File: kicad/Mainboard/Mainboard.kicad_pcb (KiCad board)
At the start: 2 copper layers, 46.9 x 107.1 mm, 275 parts, among them J1 ESP8266 module, J10 MIC_EXT, J11 VIB2, J12 SPK_EXT, J13 GPS_CONN, J14 Micro_SD_Card, J15 DBG_CONN, J3 USB_OTG, J4 SWD, J5 BATT, J6 POT_PWR_SW, J7 Conn_01x10, J8 Antenna, J9 VIB1, Q1 BSS138, Q2 BSS138, Q3 BGA6589, Q4 BSS138, Q5 BSS138, Q6 BSS138, Q7 FDV304P, SW1 INT_PTT_SW, T1 AFT05MS004NT1, U1 STM32F777VIT, U10 LM386, U11 LSM9DS1, U13 BGA2874, U2 USBLC6-2SC6, U3 LD1117S50TR_SOT223, U4 LD1117S33TR_SOT223, U5 ADF7021, U6 HMC546MS8GETR, U7 LM2904A, U8 HEF4066B, U9 OPA340UA, X1 12.288MHz

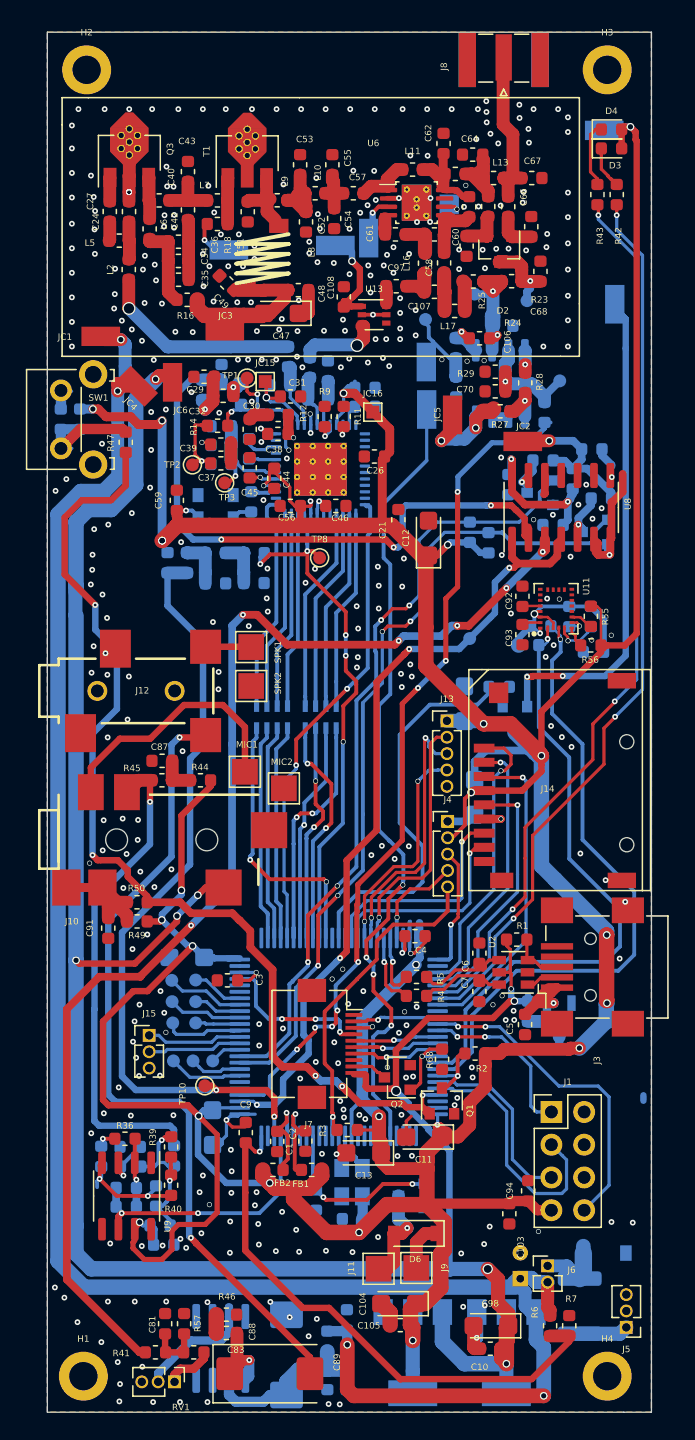
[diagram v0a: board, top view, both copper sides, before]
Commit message: added jumpers on GPIO0 and GPIO2 for ESP8266 module; described pin headers on PCB; connected pin 16 of STM32 to Power Down pin in OS1; plotted schematic in PDF
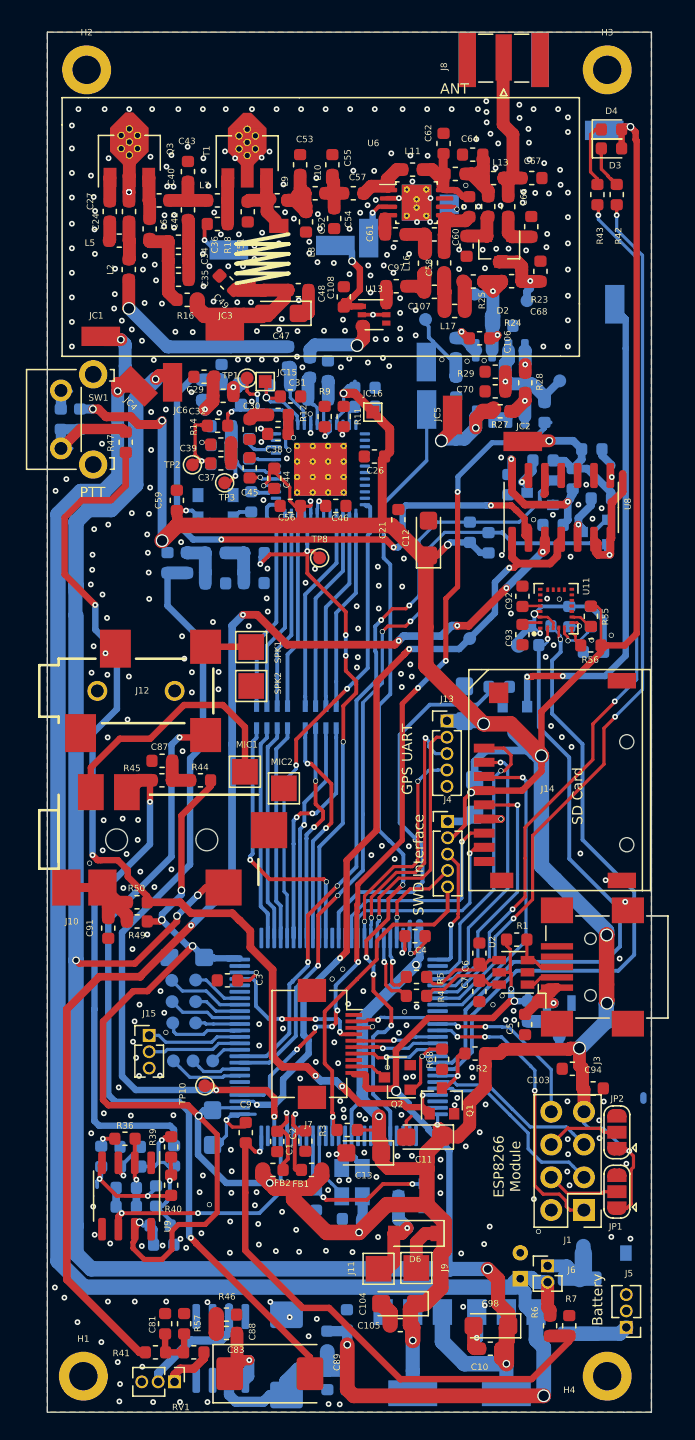
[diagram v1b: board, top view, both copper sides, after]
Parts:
- added JP1: GPIO0, Jumper:SolderJumper-3_P1.3mm_Open_RoundedPad1.0x1.5mm, F.Cu at (63.2, 158.9)
- added JP2: GPIO2, Jumper:SolderJumper-3_P1.3mm_Open_RoundedPad1.0x1.5mm, F.Cu at (63.2, 154.3)
- moved C103 12.3 mm to (59.8, 149.4), turned to 180 degrees
- moved C94 9.41 mm to (61.4, 150.9), turned to 0 degrees
- moved J1 8.02 mm to (60.7, 160.3), turned to 180 degrees
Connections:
- OS1 pad 1: Net-(OS1-Pad1) -> OscillatorON
- U1 pad 16: Net-(U1-Pad16) -> OscillatorON
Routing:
- net UART2_TX: track 25.2 -> 13.6 mm
- net UART2_RX: track 13.7 -> 23.3 mm, vias 2 -> 3
- net +3V3: track 437.4 -> 446.9 mm, vias 32 -> 33
- net Net-(J1-Pad6): track 0.00 -> 5.76 mm
- net Net-(J1-Pad4): track 0.00 -> 5.52 mm
- net OscillatorON: track 0.00 -> 5.41 mm
- net WIFI_EN: track 19.9 -> 14.9 mm
- net WIFI_RST: track 15.0 -> 14.2 mm
- net GND: vias 378 -> 433
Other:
- board text added: "ANT"
- board text added: "Battery"
- board text added: "ESP8266 Module"
- board text added: "GPS UART"
- board text added: "PTT"
- board text added: "SD Card"
- board text added: "SWD Interface"

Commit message: added more vias
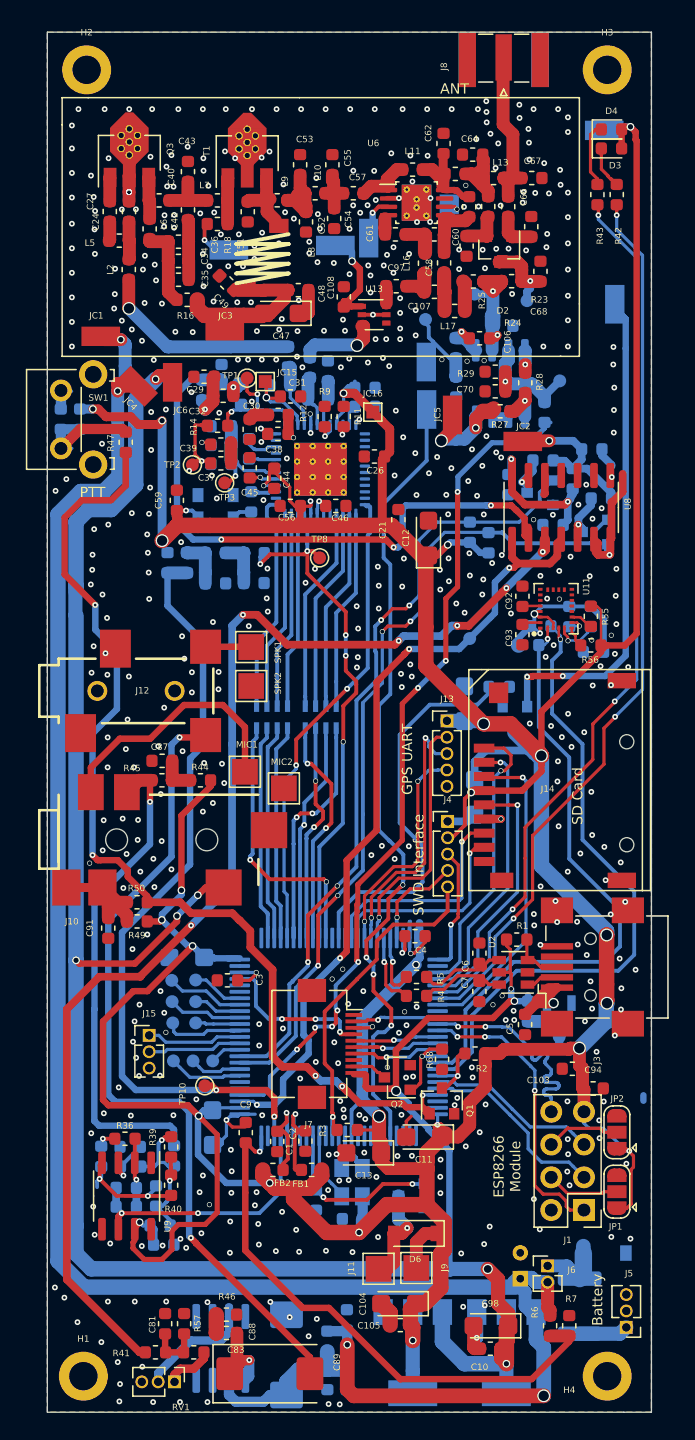
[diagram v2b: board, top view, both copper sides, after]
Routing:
- net UART2_TX: track 13.6 -> 17.8 mm
- net Net-(R13-Pad1): track 12.5 -> 10.3 mm, vias 3 -> 2
- net Net-(C29-Pad2): track 4.38 -> 3.62 mm
- net GND: vias 433 -> 530

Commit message: informations about connectors on PCB; more vias for better signal integrity; new pcb 3D photos
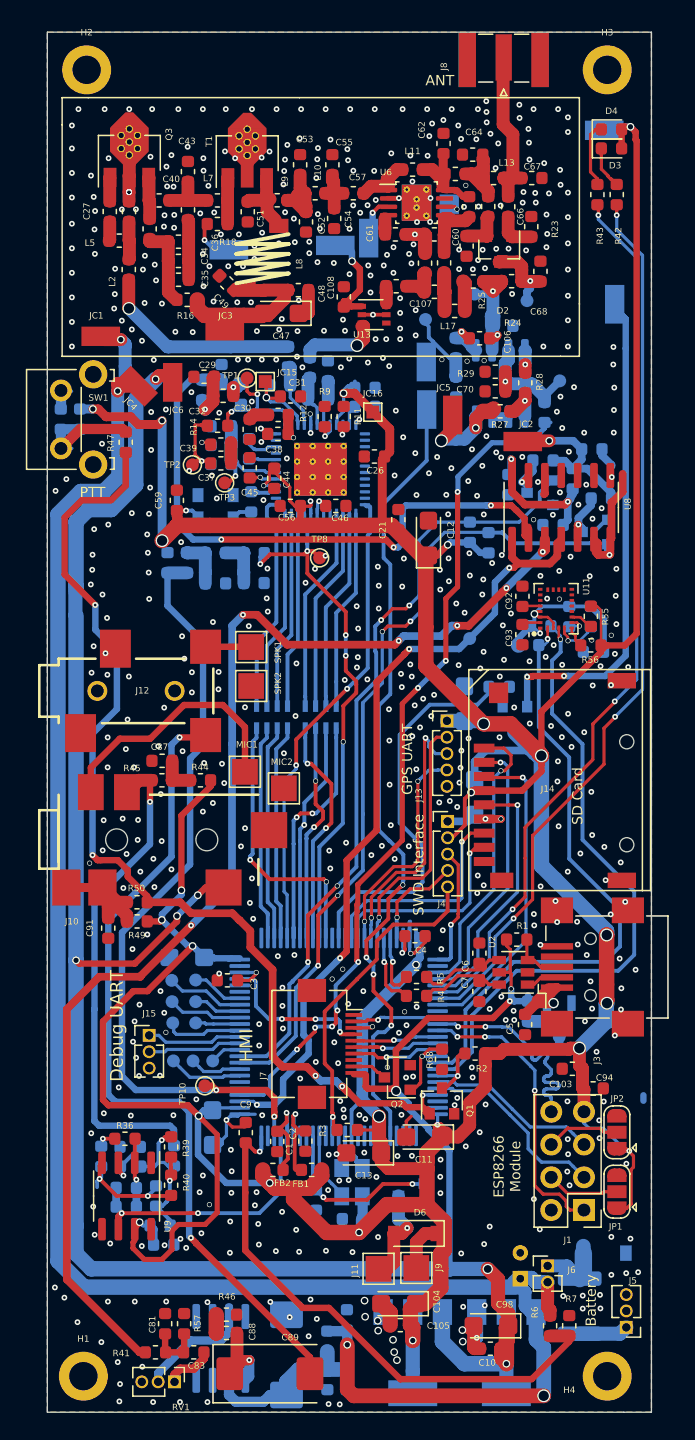
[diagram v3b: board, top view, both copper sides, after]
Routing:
- net +3V3: track 446.9 -> 445.9 mm
- net GND: vias 530 -> 632
- net ADF_SWD: vias 5 -> 6
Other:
- board text added: "Debug UART"
- board text added: "HMI"
- board text added: "bunch of not used gpios ;)"

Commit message: credit labels moved; added blank place for label
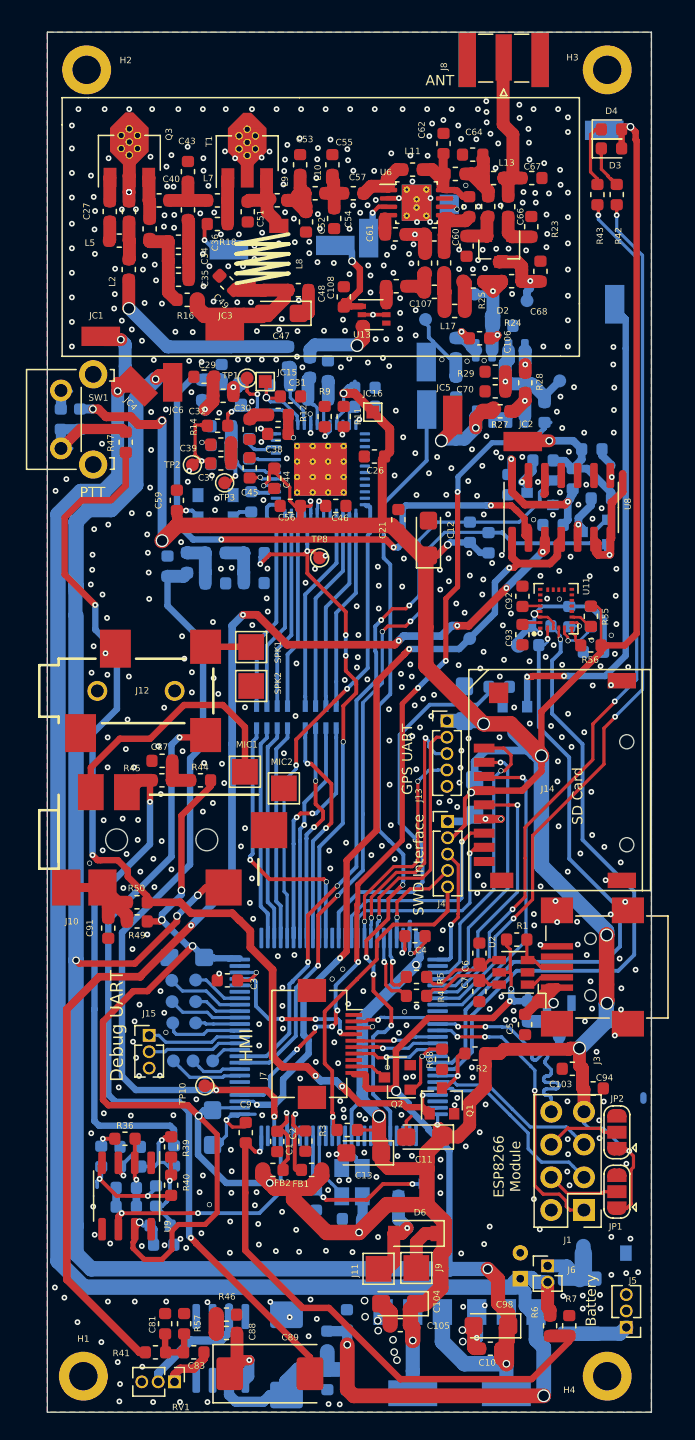
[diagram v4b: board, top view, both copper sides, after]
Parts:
- moved C95 0.27 mm to (28.4, 110.4)
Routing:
- net GND: vias 632 -> 638
- net +3V3: vias 33 -> 32
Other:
- board text added: "write something:"
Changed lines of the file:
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@@
   (general
     (thickness 1.6)
-    (drawings 64)
-    (tracks 3345)
+    (drawings 66)
+    (tracks 3351)
     (zones 0)
     (modules 277)
@@
   )
   (setup
-    (last_trace_width 0.5)
+    (last_trace_width 1)
     (user_trace_width 0.2)
     (user_trace_width 0.25)
@@
   )
   (module Capacitor_SMD:C_0603_1608Metric (layer B.Cu)
-    (at 28.3718 110.1217 270)
+    (at 28.3718 110.3885 270)
     (descr "Capacitor SMD 0603 (1608 Metric), square (rectangular) end terminal, IPC_7351 nominal, (Body size source: http://www.tortai-tech.com/upload/download/2011102023233369053.pdf), generated with kicad-footprint-generator")
     (tags capacitor)
     (attr smd)
-    (fp_text reference C95 (at -1.9177 0) (layer B.SilkS)
+    (fp_text reference C95 (at -2.7559 -0.0508) (layer B.SilkS)
       (effects (font (size 0.5 0.5) (thickness 0.15)) (justify mirror))
     )
@@
     (tags resistor)
     (attr smd)
-    (fp_text reference R19 (at 1.905 -0.0381) (layer B.SilkS)
+    (fp_text reference R19 (at 2.3241 -0.0635) (layer B.SilkS)
       (effects (font (size 0.5 0.5) (thickness 0.15)) (justify mirror))
     )
@@
     (tags capacitor)
     (attr smd)
-    (fp_text reference C72 (at 0.216 1.1557) (layer B.SilkS)
+    (fp_text reference C72 (at 0.4954 1.2319) (layer B.SilkS)
       (effects (font (size 0.5 0.5) (thickness 0.15)) (justify mirror))
     )
@@
     (tags "SMD SMT crystal")
     (attr smd)
-    (fp_text reference X1 (at -0.0762 -2.2987 180) (layer B.SilkS)
+    (fp_text reference X1 (at 0.6223 -2.1209 180) (layer B.SilkS)
       (effects (font (size 0.5 0.5) (thickness 0.15)) (justify mirror))
     )
@@
     (tags resistor)
     (attr smd)
-    (fp_text reference R10 (at -0.7874 -1.1938 90) (layer B.SilkS)
+    (fp_text reference R10 (at -1.9811 0.6604 180) (layer B.SilkS)
       (effects (font (size 0.5 0.5) (thickness 0.15)) (justify mirror))
     )
@@
     (tags resistor)
     (attr smd)
-    (fp_text reference R8 (at -0.5588 1.0668 270) (layer B.SilkS)
+    (fp_text reference R8 (at -1.8797 -0.0254) (layer B.SilkS)
       (effects (font (size 0.5 0.5) (thickness 0.15)) (justify mirror))
     )
@@
     (tags inductor)
     (attr smd)
-    (fp_text reference L14 (at -1.7779 0.2794) (layer B.SilkS)
+    (fp_text reference L14 (at -1.9178 0) (layer B.SilkS)
       (effects (font (size 0.5 0.5) (thickness 0.15)) (justify mirror))
     )
@@
     (tags "mounting hole 2.2mm m2 iso14580")
     (attr virtual)
-    (fp_text reference H2 (at 0 -2.9) (layer F.SilkS)
+    (fp_text reference H2 (at 3.03276 -0.74168) (layer F.SilkS)
       (effects (font (size 0.5 0.5) (thickness 0.15)))
     )
@@
     (tags "mounting hole 2.2mm m2 iso14580")
     (attr virtual)
-    (fp_text reference H3 (at 0 -2.9) (layer F.SilkS)
+    (fp_text reference H3 (at -2.69748 -0.96012) (layer F.SilkS)
       (effects (font (size 0.5 0.5) (thickness 0.15)))
     )
@@
     )
   )
+  (gr_text "write\nsomething:" (at 46.355 72.263) (layer B.SilkS)
+    (effects (font (size 0.7 0.7) (thickness 0.15)) (justify mirror))
+  )
+  (gr_poly (pts (xy 43.04284 74.041) (xy 25.019 74.041) (xy 25.019 70.3072) (xy 43.04284 70.3072)) (layer B.SilkS) (width 0.1))
   (gr_text "bunch of not used gpios ;)" (at 24.83612 145.37436 90) (layer B.SilkS)
     (effects (font (size 0.5 0.5) (thickness 0.125)) (justify mirror))
@@
     (effects (font (size 0.8 0.8) (thickness 0.125)))
   )
-  (gr_poly (pts (xy 47.244 130.0988) (xy 41.7576 130.0988) (xy 41.7576 127.7112) (xy 47.244 127.7112)) (layer B.SilkS) (width 0.1))
-  (gr_poly (pts (xy 47.244 126.8984) (xy 41.7576 126.8984) (xy 41.7576 124.5108) (xy 47.244 124.5108)) (layer B.SilkS) (width 0.1))
-  (gr_text "Pcb by:\nNikoloz SO3ALG" (at 33.8328 124.8664) (layer B.SilkS)
+  (gr_poly (pts (xy 47.244 130.0988) (xy 40.132 130.0988) (xy 40.132 126.9492) (xy 47.244 126.9492)) (layer B.SilkS) (width 0.1))
+  (gr_poly (pts (xy 47.244 126.8984) (xy 40.132 126.9238) (xy 40.132 124.5362) (xy 47.244 124.5108)) (layer B.SilkS) (width 0.1))
+  (gr_text "Pcb by:\nNikoloz SO3ALG" (at 37.6428 115.1636) (layer B.SilkS)
     (effects (font (size 0.7 0.7) (thickness 0.175)) (justify mirror))
   )
@@
     (effects (font (size 1.5 1.5) (thickness 0.3)))
   )
-  (gr_text TR-9 (at 29.1592 116.586) (layer B.SilkS)
+  (gr_text TR-9 (at 24.6888 115.2652) (layer B.SilkS)
     (effects (font (size 1.8 1.8) (thickness 0.28)) (justify mirror))
   )
-  (gr_text M17 (at 29.464 114.1476) (layer B.SilkS)
+  (gr_text M17 (at 25.1968 113.284) (layer B.SilkS)
     (effects (font (size 1 1) (thickness 0.15)) (justify mirror))
   )
-  (gr_text "Schematic by:\nWojtek SP5WWP,\nMathis DB9MAT et al." (at 32.4104 128.6256) (layer B.SilkS)
+  (gr_text "Schematic by:\nWojtek SP5WWP,\nMathis DB9MAT et al." (at 36.1188 118.364) (layer B.SilkS)
     (effects (font (size 0.7 0.7) (thickness 0.175)) (justify mirror))
   )
@@
   (via (at 46.57852 111.96828) (size 0.45) (drill 0.2) (layers F.Cu B.Cu) (net 1))
   (via (at 43.04792 113.49736) (size 0.45) (drill 0.2) (layers F.Cu B.Cu) (net 1))
-  (via (at 43.15968 115.22456) (size 0.45) (drill 0.2) (layers F.Cu B.Cu) (net 1))
+  (via (at 43.18 115.7224) (size 0.45) (drill 0.2) (layers F.Cu B.Cu) (net 1))
   (via (at 39.08044 111.67364) (size 0.45) (drill 0.2) (layers F.Cu B.Cu) (net 1))
   (via (at 39.81196 110.59668) (size 0.45) (drill 0.2) (layers F.Cu B.Cu) (net 1))
@@
   (via (at 36.068 112.88268) (size 0.45) (drill 0.2) (layers F.Cu B.Cu) (net 1))
   (via (at 36.14928 113.90884) (size 0.45) (drill 0.2) (layers F.Cu B.Cu) (net 1))
-  (via (at 34.67608 115.0366) (size 0.45) (drill 0.2) (layers F.Cu B.Cu) (net 1))
+  (via (at 34.9504 114.9604) (size 0.45) (drill 0.2) (layers F.Cu B.Cu) (net 1))
   (via (at 31.89732 114.72164) (size 0.45) (drill 0.2) (layers F.Cu B.Cu) (net 1))
-  (via (at 32.33928 118.5926) (size 0.45) (drill 0.2) (layers F.Cu B.Cu) (net 1))
-  (via (at 32.32404 119.9388) (size 0.45) (drill 0.2) (layers F.Cu B.Cu) (net 1))
+  (via (at 31.9532 119.0752) (size 0.45) (drill 0.2) (layers F.Cu B.Cu) (net 1))
+  (via (at 32.3088 120.2944) (size 0.45) (drill 0.2) (layers F.Cu B.Cu) (net 1))
   (via (at 23.72868 123.6726) (size 0.45) (drill 0.2) (layers F.Cu B.Cu) (net 1))
   (via (at 25.273 122.28576) (size 0.45) (drill 0.2) (layers F.Cu B.Cu) (net 1))
@@
   (segment (start 52.1132 171.0163) (end 52.1913 171.0944) (width 1) (layer F.Cu) (net 1))
   (via (at 51.27752 170.54068) (size 0.6) (drill 0.4) (layers F.Cu B.Cu) (net 1))
+  (via (at 33.3502 110.5154) (size 0.45) (drill 0.2) (layers F.Cu B.Cu) (net 1))
+  (via (at 32.512 110.5916) (size 0.45) (drill 0.2) (layers F.Cu B.Cu) (net 1))
+  (via (at 32.0548 106.045) (size 0.45) (drill 0.2) (layers F.Cu B.Cu) (net 1))
+  (via (at 29.9466 103.8352) (size 0.45) (drill 0.2) (layers F.Cu B.Cu) (net 1))
+  (via (at 31.0134 94.5388) (size 0.45) (drill 0.2) (layers F.Cu B.Cu) (net 1))
+  (via (at 30.0482 94.4626) (size 0.45) (drill 0.2) (layers F.Cu B.Cu) (net 1))
   (segment (start 37.6518 154.582) (end 37.6518 152.8662) (width 0.3) (layer B.Cu) (net 2))
   (segment (start 37.6518 152.8662) (end 37.6518 152.8154) (width 0.3) (layer B.Cu) (net 2))
@@
   (via (at 27.9527 108.4072) (size 1) (drill 0.8) (layers F.Cu B.Cu) (net 12))
   (segment (start 27.9527 108.4072) (end 27.9527 108.4072) (width 0.6) (layer B.Cu) (net 12))
-  (via (at 27.9527 108.4072) (size 0.6) (drill 0.4) (layers F.Cu B.Cu) (net 12))
   (segment (start 44.7802 153.0731) (end 44.7802 154.94) (width 1.1) (layer F.Cu) (net 12))
   (via (at 44.7802 153.0731) (size 1) (drill 0.8) (layers F.Cu B.Cu) (net 12))
@@
   (segment (start 31.8262 150.6982) (end 32.1564 151.0284) (width 0.5) (layer F.Cu) (net 121))
   (segment (start 31.2674 150.6982) (end 31.8262 150.6982) (width 0.5) (layer F.Cu) (net 121))
-  (segment (start 28.3718 110.9092) (end 29.8831 110.9092) (width 1) (layer B.Cu) (net 121))
   (segment (start 31.1277 116.2177) (end 28.3718 113.4618) (width 0.5) (layer B.Cu) (net 121))
   (segment (start 28.3718 113.4618) (end 28.3718 110.9092) (width 0.5) (layer B.Cu) (net 121))
@@
   (segment (start 32.1564 151.0284) (end 25.908 151.0284) (width 0.5) (layer B.Cu) (net 121))
   (segment (start 24.8412 149.9616) (end 24.8412 138.811) (width 0.5) (layer B.Cu) (net 121))
+  (segment (start 29.6163 111.176) (end 29.8831 110.9092) (width 1) (layer B.Cu) (net 121))
+  (segment (start 28.3718 111.176) (end 29.6163 111.176) (width 1) (layer B.Cu) (net 121))
   (via (at 57.4802 109.2708) (size 0.45) (drill 0.2) (layers F.Cu B.Cu) (net 122))
   (segment (start 57.6453 108.3026) (end 57.6453 109.1057) (width 0.8) (layer F.Cu) (net 122))
